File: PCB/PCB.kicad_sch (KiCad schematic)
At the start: 61 parts, among them J1 AudioJack3, J2 USB4105-GF-A, J4 Conn_01x09, U1 ADP151AUJZ-3.3-R7, U2 MAX41400ATB+T, U3 AD8534ARZ, U6 AD8534ARZ

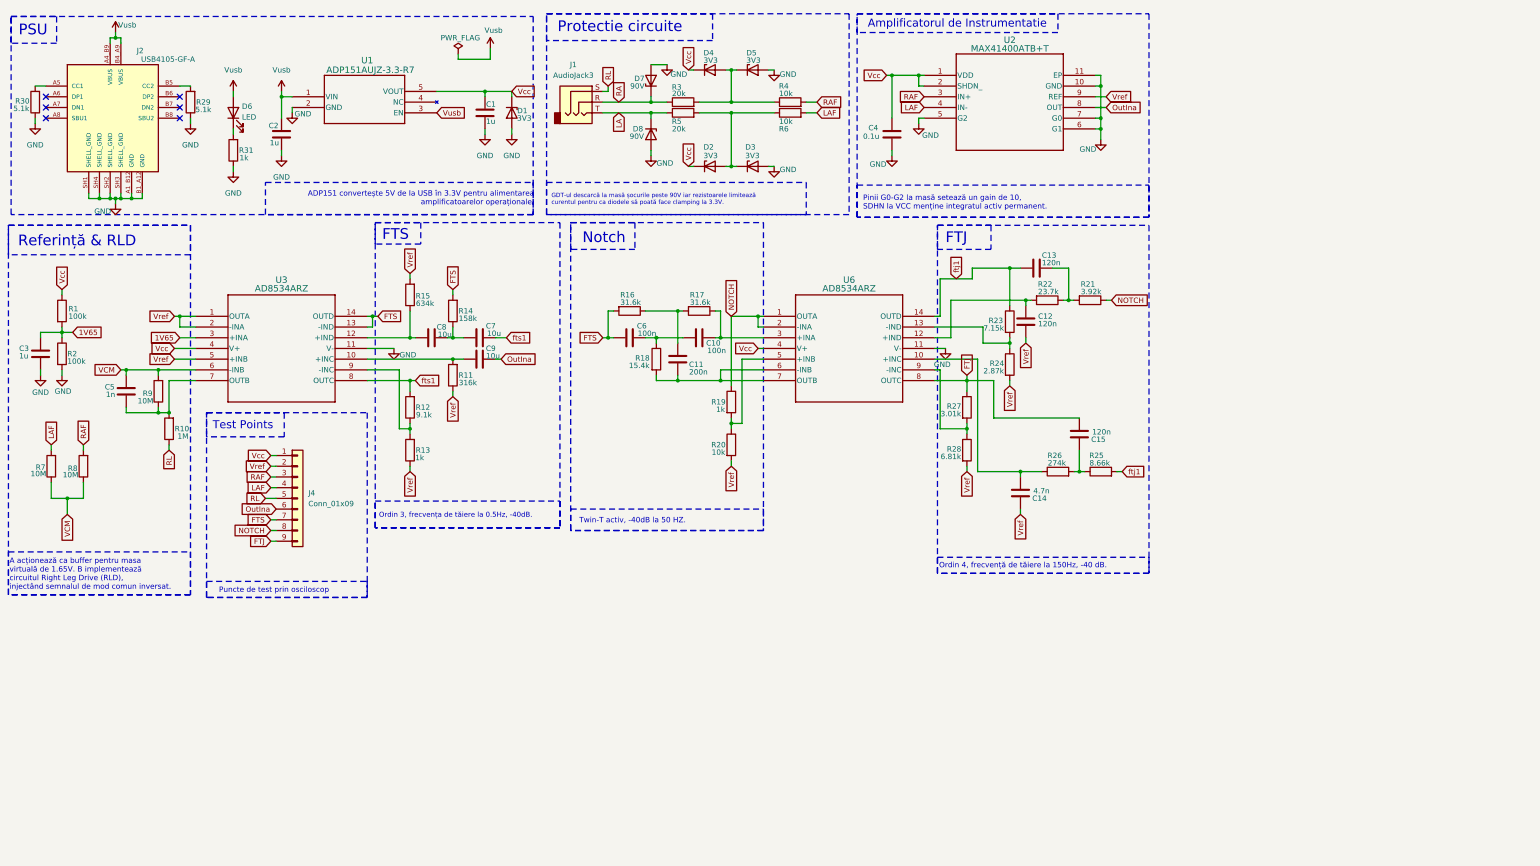
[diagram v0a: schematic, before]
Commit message: Modificat pcb ul cu scopul de a adauga test point uri
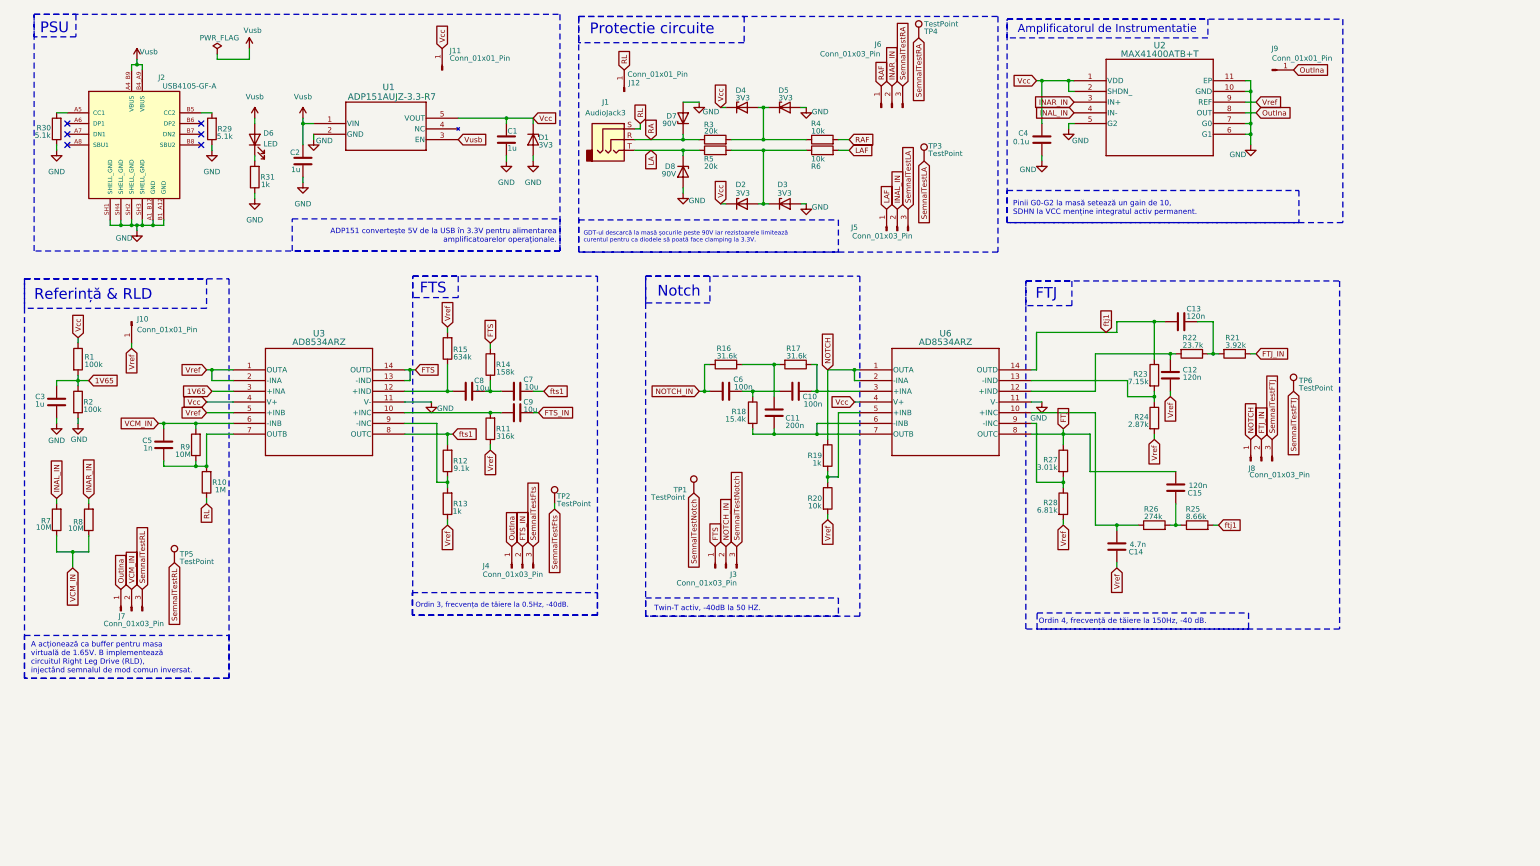
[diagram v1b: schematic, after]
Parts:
- removed J4: Conn_01x09, Connector_PinHeader_1.00mm:PinHeader_1x09_P1.00mm_Vertical, symbol Connector_Generic:Conn_01x09
- added J10, J11, J12, J9: Conn_01x01_Pin, Connector_PinHeader_2.00mm:PinHeader_1x01_P2.00mm_Vertical, symbol Connector:Conn_01x01_Pin
- added J3, J4, J5, J6, J7, J8: Conn_01x03_Pin, Connector_PinHeader_2.00mm:PinHeader_1x03_P2.00mm_Vertical, symbol Connector:Conn_01x03_Pin
- added TP1, TP2, TP3, TP4, TP5, TP6: TestPoint, TestPoint:TestPoint_Loop_D2.50mm_Drill1.0mm_LowProfile, symbol Connector:TestPoint
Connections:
- net FTS: now also J3.1 (Pin_1); no longer C6.1, R16.2
- net LAF: now also J5.1 (Pin_1); no longer R7.2, U2.4 (IN-)
- net NOTCH: now also J8.1 (Pin_1); no longer R21.1
- net OutIna: now also J4.1 (Pin_1), J7.1 (Pin_1), J9.1 (Pin_1); no longer C9.2
- net RAF: now also J6.1 (Pin_1); no longer R8.2, U2.3 (IN+)
- net RL: now also J12.1 (Pin_1)
- net Vcc: now also J11.1 (Pin_1)
- net Vref: now also J10.1 (Pin_1)
- net VCM renamed VCM_IN
- net VCM_IN: now also J7.2 (Pin_2)
- new net FTJ_IN: J8.2 (Pin_2), R21.1
- new net FTS_IN: C9.2, J4.2 (Pin_2)
- new net INAL_IN: J5.2 (Pin_2), R7.2, U2.4 (IN-)
- new net INAR_IN: J6.2 (Pin_2), R8.2, U2.3 (IN+)
- new net NOTCH_IN: C6.1, J3.2 (Pin_2), R16.2
- new net SemnalTestFTJ: J8.3 (Pin_3), TP6.1
- new net SemnalTestFts: J4.3 (Pin_3), TP2.1
- new net SemnalTestLA: J5.3 (Pin_3), TP3.1
- new net SemnalTestNotch: J3.3 (Pin_3), TP1.1
- new net SemnalTestRA: J6.3 (Pin_3), TP4.1
- new net SemnalTestRL: J7.3 (Pin_3), TP5.1
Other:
- note removed: "Puncte de test prin osciloscop"
- note removed: "Test Points"
- moved on the sheet: C1, C10, C11, C12, C13, C14, C15, C2, C3, C4, C5, C6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

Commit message: Modificat pcb
Signed-off-by: Andrei Bota <botaandrei69@yahoo.com>
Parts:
- removed J9: Conn_01x01_Pin, Connector_PinHeader_2.00mm:PinHeader_1x01_P2.00mm_Vertical, symbol Connector:Conn_01x01_Pin
- removed TP1, TP2, TP3, TP4, TP5, TP6: TestPoint, TestPoint:TestPoint_Loop_D2.50mm_Drill1.0mm_LowProfile, symbol Connector:TestPoint
- added J13, J14, J15, J16, J17, J18, J19: Conn_01x01_Pin, Connector_PinHeader_2.00mm:PinHeader_1x01_P2.00mm_Vertical, symbol Connector:Conn_01x01_Pin
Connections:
- net FTJ: now also J19.1 (Pin_1)
- net SemnalTestFTJ: now also J18.1 (Pin_1)
- net SemnalTestFts: now also J16.1 (Pin_1)
- net SemnalTestLA: now also J13.1 (Pin_1)
- net SemnalTestNotch: now also J17.1 (Pin_1)
- net SemnalTestRA: now also J14.1 (Pin_1)
- net SemnalTestRL: now also J15.1 (Pin_1)

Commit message: Remodificat un pin de testpoint
Signed-off-by: BotaAndreiD <botaandrei69@yahoo.com>
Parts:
- removed J15: Conn_01x01_Pin, Connector_PinHeader_2.00mm:PinHeader_1x01_P2.00mm_Vertical, symbol Connector:Conn_01x01_Pin
- removed J7: Conn_01x03_Pin, Connector_PinHeader_2.00mm:PinHeader_1x03_P2.00mm_Vertical, symbol Connector:Conn_01x03_Pin
- added J20, J21, J24, J7, J9: Conn_01x01_Pin, Connector_PinHeader_2.00mm:PinHeader_1x01_P2.00mm_Vertical, symbol Connector:Conn_01x01_Pin
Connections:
- net GND: now also J20.1 (Pin_1), J21.1 (Pin_1), J24.1 (Pin_1), J9.1 (Pin_1)
- net OutIna: now also J7.1 (Pin_1)

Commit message: Ultimele modificari a iteratiei A pentru PCB inainte de comanda
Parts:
- C10, C4, C6: Field5 https://ro.farnell.com/kemet/c0603c104k3ractu/cap-0-1-f-25v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 -> https://ro.farnell.com/samsung-electro-mechanics/cl10b104kb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
- C11: value 200n -> 220n; Field5 https://ro.farnell.com/samsung-electro-mechanics/cl10b224ko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 -> https://ro.farnell.com/yageo/cc0603kpx7r8bb224/cap-0-22uf-2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
- J10, J11, J12, J13, J14, J16, J17, J18, J19, J20, J21, J24, J3, J4, J5, J6, J7, J8, J9: Field5 (none) -> https://ro.farnell.com/amphenol-communications-solutions/10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
- R19: Field5 https://ro.farnell.com/panasonic/erjpb3b1001v/res-1k-0-1-0-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 -> https://ro.farnell.com/multicomp-pro/mcwr06x1001ftl/res-1k-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
- R28: Field5 https://ro.farnell.com/multicomp-pro/mcwf06r6811btl/res-6k8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 -> https://ro.farnell.com/yageo/rt0603brd076k81l/res-6k81-0-1-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
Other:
- moved on the sheet: R10
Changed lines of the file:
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@@
 	)
 	(rectangle
-		(start 256.667 156.718)
-		(end 306.832 160.528)
+		(start 254.127 156.718)
+		(end 304.292 160.528)
 		(stroke
 			(width 0)
@@
 	(text "Ordin 4, frecvență de tăiere la 150Hz, -40 dB."
 		(exclude_from_sim no)
-		(at 257.048 158.75 0)
+		(at 255.016 159.004 0)
 		(effects
 			(font
@@
 	(wire
 		(pts
-			(xy 59.69 130.81) (xy 59.69 129.54)
-		)
-		(stroke
-			(width 0)
-			(type default)
-		)
-	)
-	(wire
-		(pts
 			(xy 275.59 87.63) (xy 284.48 87.63)
 		)
@@
 	(wire
 		(pts
+			(xy 59.69 132.08) (xy 59.69 130.81)
+		)
+		(stroke
+			(width 0)
+			(type default)
+		)
+	)
+	(wire
+		(pts
 			(xy 57.15 121.92) (xy 59.69 121.92)
 		)
@@
 	(wire
 		(pts
+			(xy 59.69 123.19) (xy 59.69 121.92)
+		)
+		(stroke
+			(width 0)
+			(type default)
+		)
+	)
+	(wire
+		(pts
 			(xy 203.2 97.79) (xy 204.47 97.79)
 		)
@@
 	(global_label "RL"
 		(shape input)
-		(at 59.69 130.81 270)
+		(at 59.69 132.08 270)
 		(fields_autoplaced yes)
 		(effects
@@
 		)
 		(property "Intersheetrefs" "${INTERSHEET_REFS}"
-			(at 59.69 136.0933 90)
+			(at 59.69 137.3633 90)
 			(effects
 				(font
@@
 			)
 		)
+		(property "Field5" "https://ro.farnell.com/amphenol-communications-solutions/10138654-g04-03lf/conn-pin-header-3pos-1row-2mm/dp/3935467"
+			(at 223.52 66.04 90)
+			(effects
+				(font
+					(size 1.27 1.27)
+				)
+				(hide yes)
+			)
+		)
 		(pin "3"
 		)
@@
 			)
 		)
+		(property "Field5" "https://ro.farnell.com/amphenol-communications-solutions/10138654-g04-03lf/conn-pin-header-3pos-1row-2mm/dp/3935467"
+			(at 234.95 38.1 0)
+			(effects
+				(font
+					(size 1.27 1.27)
+				)
+				(hide yes)
+			)
+		)
 		(pin "1"
 		)
@@
 			)
 		)
+		(property "Field5" "https://ro.farnell.com/amphenol-communications-solutions/10138654-g04-03lf/conn-pin-header-3pos-1row-2mm/dp/3935467"
+			(at 171.45 123.19 0)
+			(effects
+				(font
+					(size 1.27 1.27)
+				)
+				(hide yes)
+			)
+		)
 		(pin "1"
 		)
@@
 			)
 		)
+		(property "Field5" "https://ro.farnell.com/amphenol-communications-solutions/10138654-g04-03lf/conn-pin-header-3pos-1row-2mm/dp/3935467"
+			(at 308.61 153.67 0)
+			(effects
+				(font
+					(size 1.27 1.27)
+				)
+				(hide yes)
+			)
+		)
 		(pin "1"
 		)
@@
 			)
 		)
+		(property "Field5" "https://ro.farnell.com/amphenol-communications-solutions/10138654-g04-03lf/conn-pin-header-3pos-1row-2mm/dp/3935467"
+			(at 204.47 31.75 0)
+			(effects
+				(font
+					(size 1.27 1.27)
+				)
+				(hide yes)
+			)
+		)
 		(pin "1"
 		)
@@
 			)
 		)
+		(property "Field5" "https://ro.farnell.com/amphenol-communications-solutions/10138654-g04-03lf/conn-pin-header-3pos-1row-2mm/dp/3935467"
+			(at 318.77 99.06 0)
+			(effects
+				(font
+					(size 1.27 1.27)
+				)
+				(hide yes)
+			)
+		)
 		(pin "1"
 		)
@@
 			)
 		)
+		(property "Field5" "https://ro.farnell.com/amphenol-communications-solutions/10138654-g04-03lf/conn-pin-header-3pos-1row-2mm/dp/3935467"
+			(at 115.57 27.94 90)
+			(effects
+				(font
+					(size 1.27 1.27)
+				)
+				(hide yes)
+			)
+		)
 		(pin "1"
 		)
@@
 			)
 		)
-		(property "Field5" "https://ro.farnell.com/panasonic/erjpb3b1001v/res-1k-0-1-0-2w-0603-thick-film/dp/3308229"
+		(property "Field5" "https://ro.farnell.com/multicomp-pro/mcwr06x1001ftl/res-1k-1-0-1w-0603-thick-film/dp/2447272"
 			(at 207.01 119.38 0)
 			(effects
@@
 	(symbol
 		(lib_id "Device:R")
-		(at 59.69 125.73 180)
+		(at 59.69 127 180)
 		(unit 1)
 		(exclude_from_sim no)
@@
 		(dnp no)
 		(property "Reference" "R10"
-			(at 62.738 125.73 0)
+			(at 62.738 127 0)
 			(effects
 				(font
@@
 		)
 		(property "Value" "1M"
-			(at 62.992 127.508 0)
+			(at 62.992 128.778 0)
 			(effects
 				(font
@@
 		)
 		(property "Footprint" "Resistor_SMD:R_0603_1608Metric"
-			(at 61.468 125.73 90)
+			(at 61.468 127 90)
 			(effects
 				(font
@@
 		)
 		(property "Datasheet" "~"
-			(at 59.69 125.73 0)
+			(at 59.69 127 0)
 			(effects
 				(font
@@
 		)
 		(property "Description" "Resistor"
-			(at 59.69 125.73 0)
+			(at 59.69 127 0)
 			(effects
 				(font
@@
 		)
 		(property "Field5" "https://ro.farnell.com/yageo/re0603dr-071ml/res-1m-0-5-0-1w-0603-thick-film/dp/1840601"
-			(at 59.69 125.73 0)
+			(at 59.69 127 0)
 			(effects
 				(font
@@
 		)
 		(property "Field6" ""
-			(at 59.69 125.73 0)
+			(at 59.69 127 0)
 			(effects
 				(font
@@
 			)
 		)
+		(property "Field5" "https://ro.farnell.com/amphenol-communications-solutions/10138654-g04-03lf/conn-pin-header-3pos-1row-2mm/dp/3935467"
+			(at 142.24 96.52 0)
+			(effects
+				(font
+					(size 1.27 1.27)
+				)
+				(hide yes)
+			)
+		)
 		(pin "1"
 		)
@@
 			)
 		)
+		(property "Field5" "https://ro.farnell.com/amphenol-communications-solutions/10138654-g04-03lf/conn-pin-header-3pos-1row-2mm/dp/3935467"
+			(at 222.25 36.83 90)
+			(effects
+				(font
+					(size 1.27 1.27)
+				)
+				(hide yes)
+			)
+		)
 		(pin "3"
 		)
@@
 			)
 		)
+		(property "Field5" "https://ro.farnell.com/amphenol-communications-solutions/10138654-g04-03lf/conn-pin-header-3pos-1row-2mm/dp/3935467"
+			(at 316.23 144.78 0)
+			(effects
+				(font
+					(size 1.27 1.27)
+				)
+				(hide yes)
+			)
+		)
 		(pin "1"
 		)
@@
 			)
 		)
+		(property "Field5" "https://ro.farnell.com/amphenol-communications-solutions/10138654-g04-03lf/conn-pin-header-3pos-1row-2mm/dp/3935467"
+			(at 90.17 30.48 0)
+			(effects
+				(font
+					(size 1.27 1.27)
+				)
+				(hide yes)
+			)
+		)
 		(pin "1"
 		)
@@
 			)
 		)
-		(property "Value" "200n"
+		(property "Value" "220n"
 			(at 201.422 112.268 0)
 			(effects
@@
 			)
 		)
-		(property "Field5" "https://ro.farnell.com/samsung-electro-mechanics/cl10b224ko8nnnc/cap-mlcc-0-22uf-16vdc-x7r-0603/dp/4690161"
+		(property "Field5" "https://ro.farnell.com/yageo/cc0603kpx7r8bb224/cap-0-22uf-25v-mlcc-0603/dp/3764505"
 			(at 194.31 109.22 0)
 			(effects
@@
 			)
 		)
-		(property "Field5" "https://ro.farnell.com/multicomp-pro/mcwf06r6811btl/res-6k81-0-1-0-1w-0603-thin-film/dp/2337278"
+		(property "Field5" "https://ro.farnell.com/yageo/rt0603brd076k81l/res-6k81-0-1-0-1w-0603-thin-film/dp/3496662"
 			(at 262.89 130.81 0)
 			(effects
@@
 			)
 		)
-		(property "Field5" "https://ro.farnell.com/kemet/c0603c104k3ractu/cap-0-1-f-25v-10-x7r-0603/dp/1650835"
+		(property "Field5" "https://ro.farnell.com/samsung-electro-mechanics/cl10b104kb8nnnc/capacitor-mlcc-0-1uf-x7r-50v-0603/dp/4539043"
 			(at 182.88 104.14 90)
 			(effects
@@
 			)
 		)
+		(property "Field5" "https://ro.farnell.com/amphenol-communications-solutions/10138654-g04-03lf/conn-pin-header-3pos-1row-2mm/dp/3935467"
+			(at 311.15 31.75 90)
+			(effects
+				(font
+					(size 1.27 1.27)
+				)
+				(hide yes)
+			)
+		)
 		(pin "1"
 		)
@@
 			)
 		)
+		(property "Field5" "https://ro.farnell.com/amphenol-communications-solutions/10138654-g04-03lf/conn-pin-header-3pos-1row-2mm/dp/3935467"
+			(at 158.75 33.02 90)
+			(effects
+				(font
+					(size 1.27 1.27)
+				)
+				(hide yes)
+			)
+		)
 		(pin "1"
 		)
@@
 			)
 		)
+		(property "Field5" "https://ro.farnell.com/amphenol-communications-solutions/10138654-g04-03lf/conn-pin-header-3pos-1row-2mm/dp/3935467"
+			(at 182.88 146.05 90)
+			(effects
+				(font
+					(size 1.27 1.27)
+				)
+				(hide yes)
+			)
+		)
 		(pin "3"
 		)
@@
 			)
 		)
-		(property "Field5" "https://ro.farnell.com/kemet/c0603c104k3ractu/cap-0-1-f-25v-10-x7r-0603/dp/1650835"
+		(property "Field5" "https://ro.farnell.com/samsung-electro-mechanics/cl10b104kb8nnnc/capacitor-mlcc-0-1uf-x7r-50v-0603/dp/4539043"
 			(at 199.39 104.14 90)
 			(effects
@@
 			)
 		)
+		(property "Field5" "https://ro.farnell.com/amphenol-communications-solutions/10138654-g04-03lf/conn-pin-header-3pos-1row-2mm/dp/3935467"
+			(at 144.78 124.46 0)
+			(effects
+				(font
+					(size 1.27 1.27)
+				)
+				(hide yes)
+			)
+		)
 		(pin "1"
 		)
@@
 			)
 		)
-		(property "Field5" "https://ro.farnell.com/kemet/c0603c104k3ractu/cap-0-1-f-25v-10-x7r-0603/dp/1650835"
+		(property "Field5" "https://ro.farnell.com/samsung-electro-mechanics/cl10b104kb8nnnc/capacitor-mlcc-0-1uf-x7r-50v-0603/dp/4539043"
 			(at 257.81 44.45 0)
 			(effects
@@
 			)
 		)
+		(property "Field5" "https://ro.farnell.com/amphenol-communications-solutions/10138654-g04-03lf/conn-pin-header-3pos-1row-2mm/dp/3935467"
+			(at 41.91 87.63 90)
+			(effects
+				(font
+					(size 1.27 1.27)
+				)
+				(hide yes)
+			)
+		)
 		(pin "1"
 		)
@@
 			)
 		)
+		(property "Field5" "https://ro.farnell.com/amphenol-communications-solutions/10138654-g04-03lf/conn-pin-header-3pos-1row-2mm/dp/3935467"
+			(at 234.95 48.26 0)
+			(effects
+				(font
+					(size 1.27 1.27)
+				)
+				(hide yes)
+			)
+		)
 		(pin "1"
 		)
@@
 			)
 		)
+		(property "Field5" "https://ro.farnell.com/amphenol-communications-solutions/10138654-g04-03lf/conn-pin-header-3pos-1row-2mm/dp/3935467"
+			(at 309.88 120.65 90)
+			(effects
+				(font
+					(size 1.27 1.27)
+				)
+				(hide yes)
+			)
+		)
 		(pin "3"
 		)
@@
 			(effects
 				(font
+					(size 1.27 1.27)
+				)
+				(hide yes)
+			)
+		)
+		(property "Field5" "https://ro.farnell.com/amphenol-communications-solutions/10138654-g04-03lf/conn-pin-header-3pos-1row-2mm/dp/3935467"
+			(at 134.62 146.05 90)
+			(effects
+				(font

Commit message: Adaugat adc si uc la pcb
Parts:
- added C16, C17, C19, C20, C21: 100n, Capacitor_SMD:C_1206_3216Metric_Pad1.33x1.80mm_HandSolder, symbol Device:C
- added C18: 1u, Capacitor_SMD:C_1206_3216Metric_Pad1.33x1.80mm_HandSolder, symbol Device:C
- added J15: Conn_01x03_Pin, Connector_PinSocket_2.54mm:PinSocket_1x08_P2.54mm_Vertical, symbol Connector:Conn_01x03_Pin
- added U4: AD7124-4BRUZ, footprints:RU-24_ADI-L, symbol 2026-04-04_06-11-20:AD7124-4BRUZ
- added U5: ESP32-C3_SUPERMINI_TH, footprints:MODULE_ESP32-C3_SUPERMINI_TH, symbol ESP32:ESP32-C3_SUPERMINI_TH
- C1, C10, C11, C12, C13, C14, C15, C2, C3, C4, C5, C6, C7, C8, C9: footprint Capacitor_SMD:C_0603_1608Metric -> Capacitor_SMD:C_1206_3216Metric_Pad1.33x1.80mm_HandSolder
- J10, J11, J12, J13, J14, J16, J17, J18, J19, J20, J21, J24, J7, J9: footprint Connector_PinHeader_2.00mm:PinHeader_1x01_P2.00mm_Vertical -> Connector_PinHeader_2.54mm:PinHeader_1x03_P2.54mm_Vertical
- J3, J4, J5, J6, J8: footprint Connector_PinHeader_2.00mm:PinHeader_1x03_P2.00mm_Vertical -> Connector_PinHeader_2.54mm:PinHeader_1x03_P2.54mm_Vertical
- R1, R10, R11, R12, R13, R14, R15, R16, R17, R18, R19, R2, R20, R21, R22, R23, R24, R25, R26, R27, R29, R3, R30, R31, R4, R5, R6, R7, R8, R9: footprint Resistor_SMD:R_0603_1608Metric -> Resistor_SMD:R_1206_3216Metric_Pad1.30x1.75mm_HandSolder
- R28: footprint Resistor_SMD:R_0603_1608Metric -> Capacitor_SMD:C_0603_1608Metric
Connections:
- net FTJ: now also U4.8 (AIN0/IOUT/VBIAS)
- net GND: now also C16.2, C17.2, C18.2, C19.2, C20.2, C21.2, U4.19 (AVSS), U4.21 (PSW), U4.3 (CLK), U4.7 (DGND), U5.G (GND)
- net Vcc: now also C18.1, C19.1, C20.1, C21.1, U4.22 (AVDD), U4.23 (*SYNC), U4.6 (IOVDD), U5.3.3 (3V3)
- net Vref: now also U4.9 (AIN1/IOUT/VBIAS)
- net Vusb: now also U5.5V
- net LAF renamed DCPOT-
- net DCPOT-: now also U4.11 (AIN3/IOUT/VBIAS/P2)
- net RAF renamed DCPOT+
- net DCPOT+: now also U4.10 (AIN2/IOUT/VBIAS/P1)
- new net: C17.1, U4.5 (REGCAPD)
- new net: C16.1, U4.20 (REGCAPA)
- new net CS: U4.4 (*CS), U5.7 (GPIO7)
- new net MISO: U4.24 (DOUT/*RDY), U5.5 (GPIO5)
- new net MOSI: U4.1 (DIN), U5.6 (GPIO6)
- new net SCK: U4.2 (SCLK), U5.4 (GPIO4)
- no-connect marks 6 -> 22
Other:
- moved on the sheet: J13, J14, J5, J6
